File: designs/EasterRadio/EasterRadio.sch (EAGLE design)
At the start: 73 parts, among them IC1 MCP73832T-2ACI_OT, IC2 LD117ADT-TR, IC3 DMP1045U-7, IC6 ESP32-WROVER-B, J1 S2B-NSHSS-TB, J2 S2B-NSHSS-TB, J3 S2B-NSHSS-TB, J4 S2B-PH-SM4, J5 S2B-NSHSS-TB, J6 PJ-002AH-SMT-TR, Q1 2SC3838T146, Y1 32.768kHz crystal

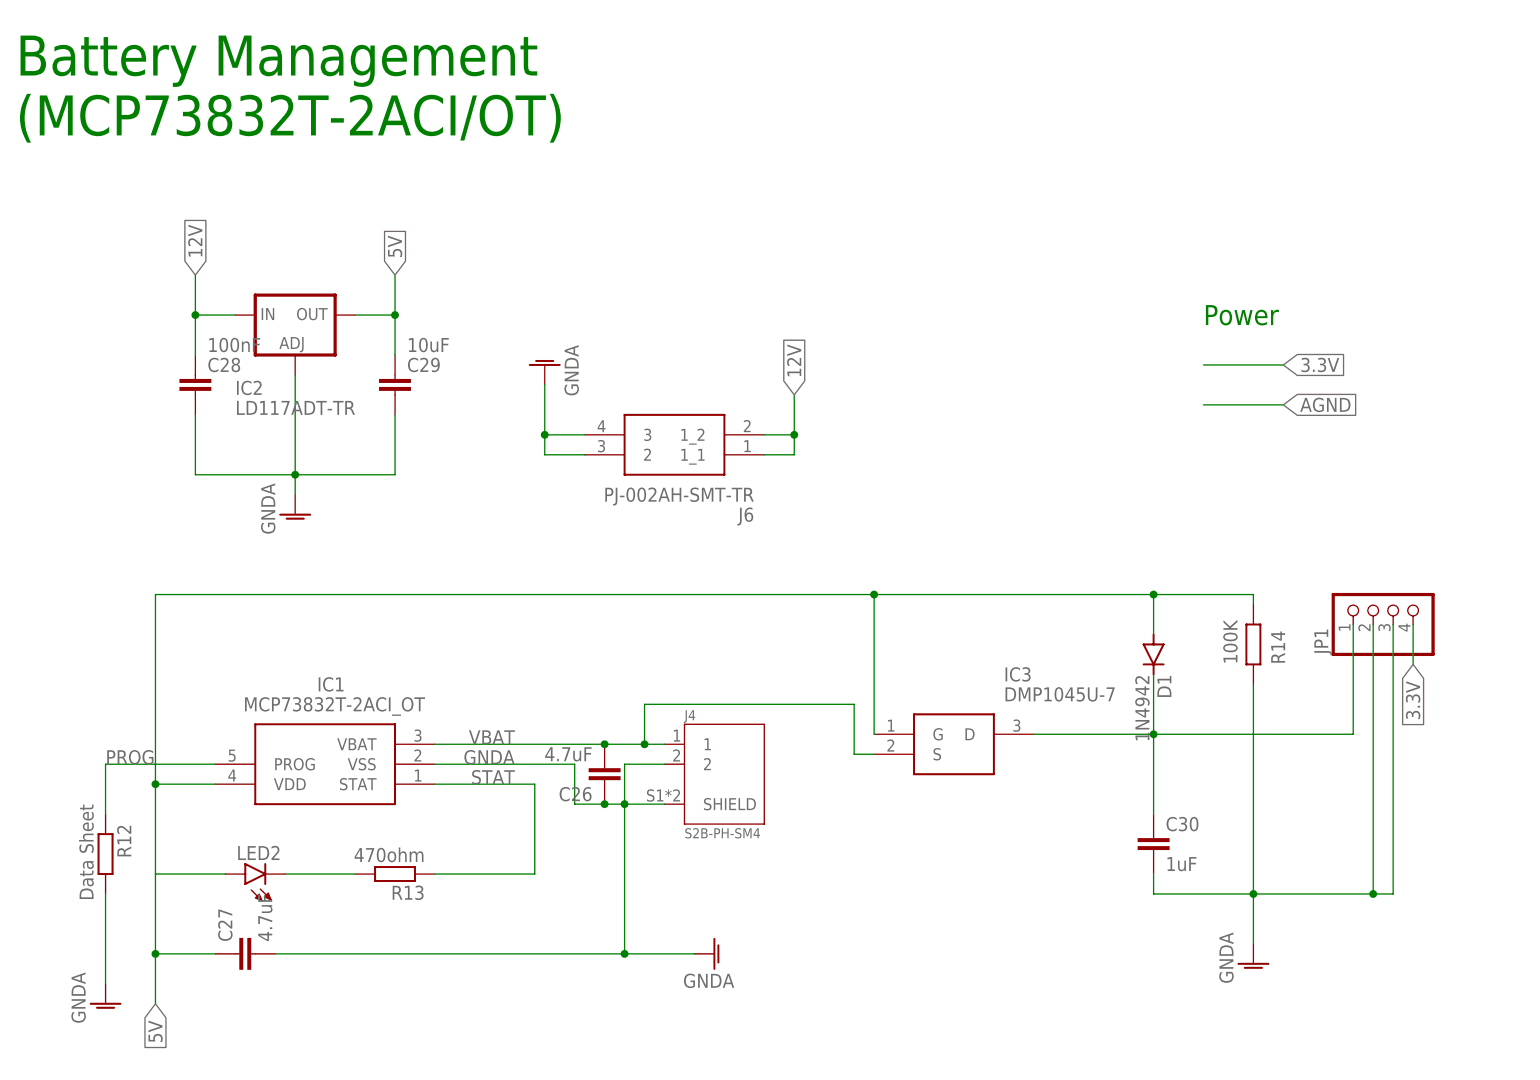
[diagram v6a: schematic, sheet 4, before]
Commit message: removed 12V to 5V voltage regulator and added singel sch and brd for power
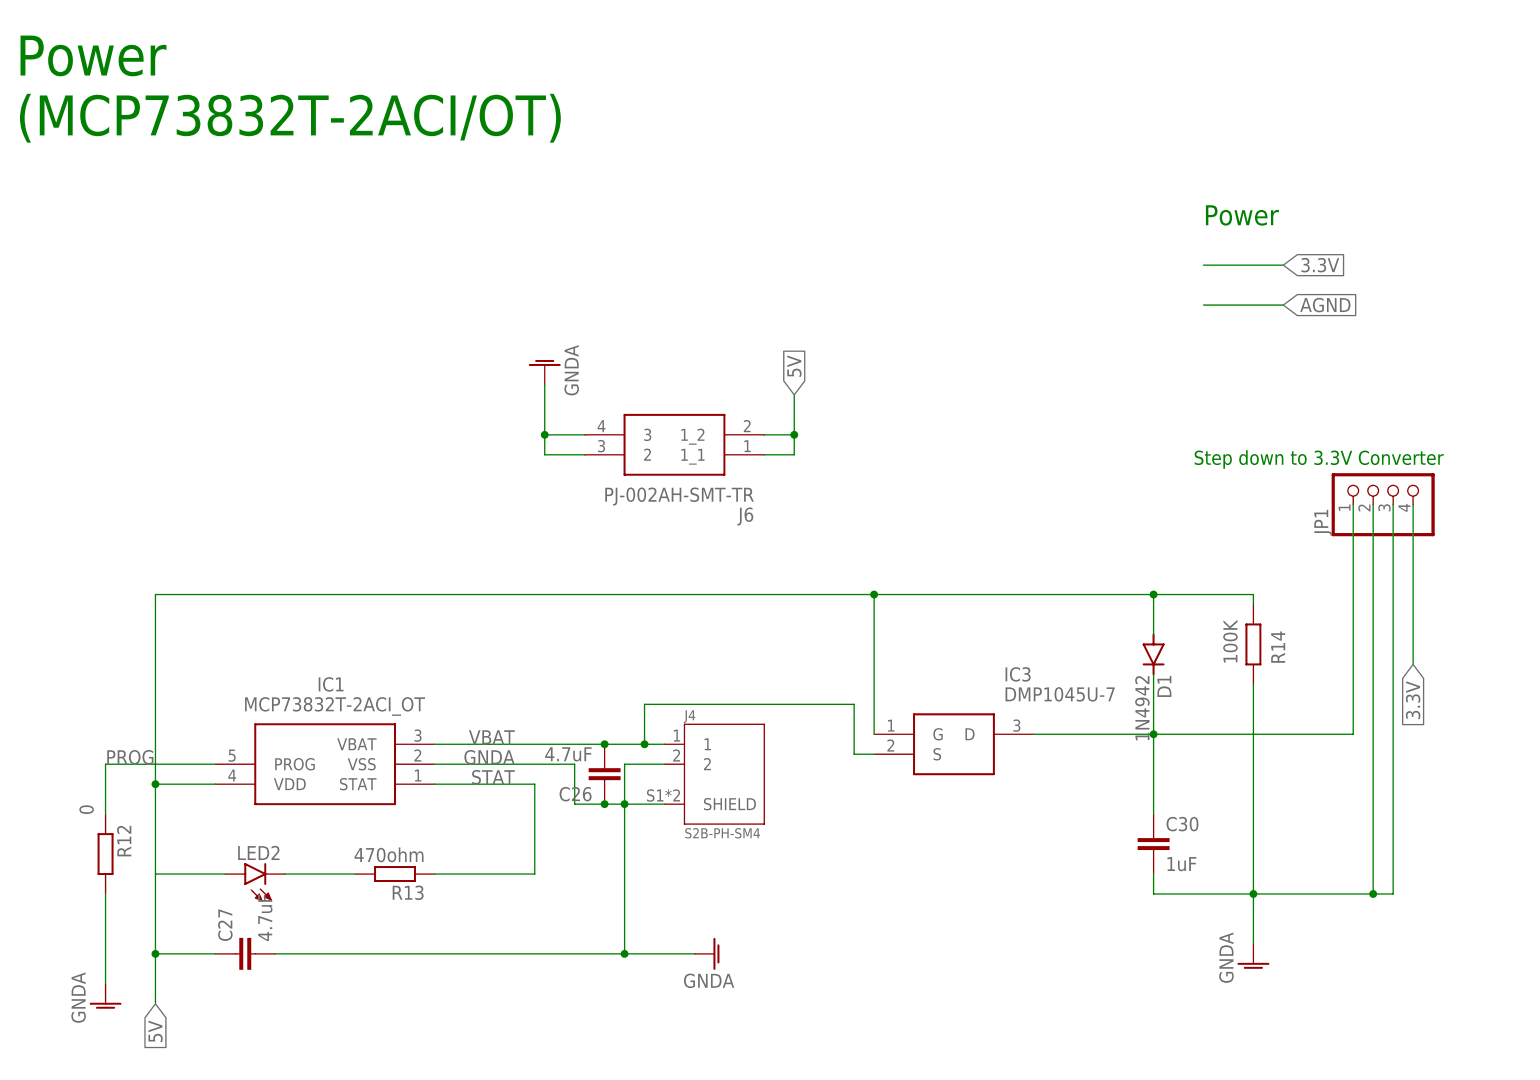
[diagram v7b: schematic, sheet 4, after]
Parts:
- removed C28: 100nF, CommonParts:C-EU_1206C1206
- removed C29: 10uF, CommonParts:C-EU_1206C1206
- removed IC2: LD117ADT-TR, nixie_tube:LD117ADT-TR
- R12: value Data Sheet -> 0
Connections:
- net 12V: no longer C28.1, IC2.IN
- net 5V: no longer C29.1, IC2.OUT
- net GNDA: no longer C28.2, C29.2, IC2.ADJ
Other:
- note added: "Power (MCP73832T-2ACI/OT)"
- note added: "Step down to 3.3V Converter"
- note removed: "Battery Management (MCP73832T-2ACI/OT)"
- moved on the sheet: JP1
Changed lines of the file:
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@@
 <setting verticaltext="up"/>
 </settings>
-<grid distance="0.05" unitdist="inch" unit="inch" style="dots" multiple="1" display="yes" altdistance="0.01" altunitdist="inch" altunit="inch"/>
+<grid distance="0.1" unitdist="inch" unit="inch" style="lines" multiple="1" display="no" altdistance="0.01" altunitdist="inch" altunit="inch"/>
 <layers>
 <layer number="1" name="Top" color="4" fill="1" visible="no" active="no"/>
@@
 <classes>
 <class number="0" name="default" width="0" drill="0">
+<clearance class="0" value="0.205"/>
 </class>
 <class number="1" name="other" width="0.2" drill="0.2">
-<clearance class="1" value="0.1"/>
+<clearance class="0" value="0.205"/>
+<clearance class="1" value="0.205"/>
 </class>
 </classes>
@@
 <part name="J4" library="CommonParts" deviceset="S2B-PH-SM4" device=""/>
 <part name="C26" library="CommonParts" deviceset="C-EU_1206" device="C1206" package3d_urn="urn:adsk.eagle:package:23618/2" value="4.7uF"/>
-<part name="R12" library="CommonParts" deviceset="R-EU_1206" device="R1206" package3d_urn="urn:adsk.eagle:package:23540/2" value="Data Sheet"/>
+<part name="R12" library="CommonParts" deviceset="R-EU_1206" device="R1206" package3d_urn="urn:adsk.eagle:package:23540/2" value="0"/>
 <part name="GND3" library="supply1" library_urn="urn:adsk.eagle:library:371" deviceset="GNDA" device=""/>
 <part name="R13" library="CommonParts" deviceset="R-EU_1206" device="R1206" package3d_urn="urn:adsk.eagle:package:23540/2" value="470ohm"/>
@@
 <part name="C27" library="CommonParts" deviceset="C-EU_1206" device="C1206" package3d_urn="urn:adsk.eagle:package:23618/2" value="4.7uF"/>
 <part name="GND4" library="supply1" library_urn="urn:adsk.eagle:library:371" deviceset="GNDA" device=""/>
-<part name="IC2" library="nixie_tube" deviceset="LD117A?*" device="DT" package3d_urn="urn:adsk.eagle:package:30369/1" technology="-TR"/>
-<part name="C28" library="CommonParts" deviceset="C-EU_1206" device="C1206" package3d_urn="urn:adsk.eagle:package:23618/2" value="100nF"/>
-<part name="C29" library="CommonParts" deviceset="C-EU_1206" device="C1206" package3d_urn="urn:adsk.eagle:package:23618/2" value="10uF"/>
-<part name="GND5" library="supply1" library_urn="urn:adsk.eagle:library:371" deviceset="GNDA" device=""/>
 <part name="J6" library="CommonParts" deviceset="PJ-002AH-SMT-TR" device=""/>
 <part name="GND6" library="supply1" library_urn="urn:adsk.eagle:library:371" deviceset="GNDA" device=""/>
@@
 <sheet>
 <plain>
-<text x="0" y="120.65" size="5.08" layer="91">Battery Management
+<text x="0" y="120.65" size="5.08" layer="91">Power
 (MCP73832T-2ACI/OT)</text>
-<text x="151.13" y="96.52" size="2.54" layer="91">Power</text>
+<text x="151.13" y="109.22" size="2.54" layer="91">Power</text>
 <frame x1="0" y1="0" x2="186.69" y2="118.11" columns="8" rows="5" layer="91"/>
+<text x="149.86" y="78.74" size="1.778" layer="91">Step down to 3.3V Converter</text>
 </plain>
 <instances>
@@
 <attribute name="VALUE" x="91.44" y="13.97" size="1.778" layer="96" rot="R180"/>
 </instance>
-<instance part="IC2" gate="G$1" x="35.56" y="97.79" smashed="yes">
-<attribute name="NAME" x="27.94" y="87.63" size="1.778" layer="95"/>
-<attribute name="VALUE" x="27.94" y="85.09" size="1.778" layer="96"/>
-</instance>
-<instance part="C28" gate="G$1" x="22.86" y="90.17" smashed="yes">
-<attribute name="NAME" x="24.384" y="90.551" size="1.778" layer="95"/>
-<attribute name="VALUE" x="24.384" y="93.091" size="1.778" layer="96"/>
-</instance>
-<instance part="C29" gate="G$1" x="48.26" y="90.17" smashed="yes">
-<attribute name="NAME" x="49.784" y="90.551" size="1.778" layer="95"/>
-<attribute name="VALUE" x="49.784" y="93.091" size="1.778" layer="96"/>
-</instance>
-<instance part="GND5" gate="1" x="35.56" y="72.39" smashed="yes">
-<attribute name="VALUE" x="33.02" y="69.85" size="1.778" layer="96" rot="R90"/>
-</instance>
 <instance part="J6" gate="G$1" x="95.25" y="80.01" smashed="yes" rot="R180">
 <attribute name="NAME" x="93.98" y="72.39" size="1.778" layer="95" rot="R180" align="center-left"/>
@@
 <attribute name="VALUE" x="69.85" y="93.98" size="1.778" layer="96" rot="R270"/>
 </instance>
-<instance part="JP1" gate="A" x="175.26" y="60.96" smashed="yes" rot="R90">
-<attribute name="NAME" x="167.005" y="54.61" size="1.778" layer="95" rot="R90"/>
-<attribute name="VALUE" x="182.88" y="54.61" size="1.778" layer="96" rot="R90"/>
+<instance part="JP1" gate="A" x="175.26" y="76.2" smashed="yes" rot="R90">
+<attribute name="NAME" x="167.005" y="69.85" size="1.778" layer="95" rot="R90"/>
+<attribute name="VALUE" x="182.88" y="69.85" size="1.778" layer="96" rot="R90"/>
 </instance>
 <instance part="IC3" gate="G$1" x="109.22" y="44.45" smashed="yes">
@@
 </segment>
 <segment>
-<pinref part="C28" gate="G$1" pin="2"/>
-<wire x1="22.86" y1="85.09" x2="22.86" y2="77.47" width="0.1524" layer="91"/>
-<wire x1="22.86" y1="77.47" x2="35.56" y2="77.47" width="0.1524" layer="91"/>
-<pinref part="IC2" gate="G$1" pin="ADJ"/>
-<wire x1="35.56" y1="77.47" x2="35.56" y2="90.17" width="0.1524" layer="91"/>
-<junction x="35.56" y="77.47"/>
-<pinref part="C29" gate="G$1" pin="2"/>
-<wire x1="35.56" y1="77.47" x2="48.26" y2="77.47" width="0.1524" layer="91"/>
-<wire x1="48.26" y1="77.47" x2="48.26" y2="85.09" width="0.1524" layer="91"/>
-<pinref part="GND5" gate="1" pin="GNDA"/>
-<wire x1="35.56" y1="74.93" x2="35.56" y2="77.47" width="0.1524" layer="91"/>
-</segment>
-<segment>
 <pinref part="J6" gate="G$1" pin="2"/>
 <wire x1="72.39" y1="80.01" x2="67.31" y2="80.01" width="0.1524" layer="91"/>
@@
 <pinref part="GND9" gate="1" pin="GNDA"/>
 <pinref part="JP1" gate="A" pin="2"/>
-<wire x1="172.72" y1="58.42" x2="172.72" y2="24.13" width="0.1524" layer="91"/>
+<wire x1="172.72" y1="73.66" x2="172.72" y2="24.13" width="0.1524" layer="91"/>
 <wire x1="172.72" y1="24.13" x2="157.48" y2="24.13" width="0.1524" layer="91"/>
 <pinref part="JP1" gate="A" pin="3"/>
-<wire x1="175.26" y1="58.42" x2="175.26" y2="24.13" width="0.1524" layer="91"/>
+<wire x1="175.26" y1="73.66" x2="175.26" y2="24.13" width="0.1524" layer="91"/>
 <wire x1="175.26" y1="24.13" x2="172.72" y2="24.13" width="0.1524" layer="91"/>
 <junction x="172.72" y="24.13"/>
@@
 </net>
 <net name="12V" class="0">
-<segment>
-<pinref part="C28" gate="G$1" pin="1"/>
-<wire x1="22.86" y1="92.71" x2="22.86" y2="97.79" width="0.1524" layer="91"/>
-<pinref part="IC2" gate="G$1" pin="IN"/>
-<wire x1="22.86" y1="97.79" x2="27.94" y2="97.79" width="0.1524" layer="91"/>
-<wire x1="22.86" y1="97.79" x2="22.86" y2="102.87" width="0.1524" layer="91"/>
-<junction x="22.86" y="97.79"/>
-<label x="22.86" y="102.87" size="1.778" layer="95" rot="R90" xref="yes"/>
-</segment>
 <segment>
 <pinref part="J6" gate="G$1" pin="1_2"/>
@@
 </segment>
 <segment>
-<label x="99.06" y="87.63" size="1.778" layer="95" rot="R90" xref="yes"/>
-</segment>
-<segment>
 <pinref part="JP1" gate="A" pin="1"/>
 <pinref part="IC3" gate="G$1" pin="D"/>
@@
 <wire x1="144.78" y1="44.45" x2="144.78" y2="34.29" width="0.1524" layer="91"/>
 <junction x="144.78" y="44.45"/>
-<wire x1="170.18" y1="58.42" x2="170.18" y2="44.45" width="0.1524" layer="91"/>
+<wire x1="170.18" y1="73.66" x2="170.18" y2="44.45" width="0.1524" layer="91"/>
 <wire x1="170.18" y1="44.45" x2="144.78" y2="44.45" width="0.1524" layer="91"/>
 <pinref part="C30" gate="G$1" pin="1"/>
@@
 </segment>
 <segment>
-<pinref part="IC2" gate="G$1" pin="OUT"/>
-<pinref part="C29" gate="G$1" pin="1"/>
-<wire x1="43.18" y1="97.79" x2="48.26" y2="97.79" width="0.1524" layer="91"/>
-<wire x1="48.26" y1="97.79" x2="48.26" y2="92.71" width="0.1524" layer="91"/>
-<wire x1="48.26" y1="97.79" x2="48.26" y2="102.87" width="0.1524" layer="91"/>
-<junction x="48.26" y="97.79"/>
-<label x="48.26" y="102.87" size="1.778" layer="95" rot="R90" xref="yes"/>
+<label x="99.06" y="87.63" size="1.778" layer="95" rot="R90" xref="yes"/>
 </segment>
 </net>
@@
 <segment>
 <pinref part="JP1" gate="A" pin="4"/>
-<wire x1="177.8" y1="58.42" x2="177.8" y2="53.34" width="0.1524" layer="91"/>
+<wire x1="177.8" y1="73.66" x2="177.8" y2="53.34" width="0.1524" layer="91"/>
 <label x="177.8" y="53.34" size="1.778" layer="95" rot="R270" xref="yes"/>
 </segment>
 <segment>
-<wire x1="151.13" y1="91.44" x2="161.29" y2="91.44" width="0.1524" layer="91"/>
-<label x="161.29" y="91.44" size="1.778" layer="95" xref="yes"/>
+<wire x1="151.13" y1="104.14" x2="161.29" y2="104.14" width="0.1524" layer="91"/>
+<label x="161.29" y="104.14" size="1.778" layer="95" xref="yes"/>
 </segment>
 </net>
 <net name="AGND" class="0">
 <segment>
-<wire x1="151.13" y1="86.36" x2="161.29" y2="86.36" width="0.1524" layer="91"/>
-<label x="161.29" y="86.36" size="1.778" layer="95" xref="yes"/>
-</segment>
-</net>
+<wire x1="151.13" y1="99.06" x2="161.29" y2="99.06" width="0.1524" layer="91"/>
+<label x="161.29" y="99.06" size="1.778" layer="95" xref="yes"/>
+</segment>
+</net>
